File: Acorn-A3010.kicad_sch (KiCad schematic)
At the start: 0 parts

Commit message: progress schematic
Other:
- added sheet Audio (audio.kicad_sch)
- added sheet Keyboard (keyboard.kicad_sch)
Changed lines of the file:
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@@
+	)
+	(sheet
+		(at 109.22 82.55)
+		(size 21.59 17.78)
+		(fields_autoplaced yes)
+		(stroke
+			(width 0.1524)
+			(type solid)
+		)
+		(fill
+			(color 0 0 0 0.0000)
+		)
+		(property "Sheetname" "Audio"
+			(at 109.22 81.8384 0)
+			(effects
+				(font
+					(size 1.27 1.27)
+				)
+				(justify left bottom)
+			)
+		)
+		(property "Sheetfile" "audio.kicad_sch"
+			(at 109.22 100.9146 0)
+			(effects
+				(font
+					(size 1.27 1.27)
+				)
+				(justify left top)
+			)
+		)
+		(instances
+			(project "Acorn-A3010"
+				(path "/999882f3-94f8-4a89-9093-27a47d0cb289"
+					(page "13")
+				)
+			)
+		)
 	)
 	(sheet
@@
 	)
 	(sheet
+		(at 133.35 127)
+		(size 21.59 16.51)
+		(fields_autoplaced yes)
+		(stroke
+			(width 0.1524)
+			(type solid)
+		)
+		(fill
+			(color 0 0 0 0.0000)
+		)
+		(property "Sheetname" "Keyboard"
+			(at 133.35 126.2884 0)
+			(effects
+				(font
+					(size 1.27 1.27)
+				)
+				(justify left bottom)
+			)
+		)
+		(property "Sheetfile" "keyboard.kicad_sch"
+			(at 133.35 144.0946 0)
+			(effects
+				(font
+					(size 1.27 1.27)
+				)
+				(justify left top)
+			)
+		)
+		(instances
+			(project "Acorn-A3010"
+				(path "/999882f3-94f8-4a89-9093-27a47d0cb289"
+					(page "12")
+				)
+			)
+		)
+	)
+	(sheet
 		(at 186.69 95.25)
 		(size 22.225 20.32)
@@
 	)
 	(sheet
-		(at 109.22 82.55)
+		(at 85.09 82.55)
 		(size 21.59 17.78)
 		(fields_autoplaced yes)
@@
 		)
 		(property "Sheetname" "Reset"
-			(at 109.22 81.8384 0)
+			(at 85.09 81.8384 0)
 			(effects
 				(font
@@
 		)
 		(property "Sheetfile" "reset.kicad_sch"
-			(at 109.22 100.9146 0)
-			(effects
-				(font
+			(at 85.09 100.9146 0)
+			(effects
+				(font

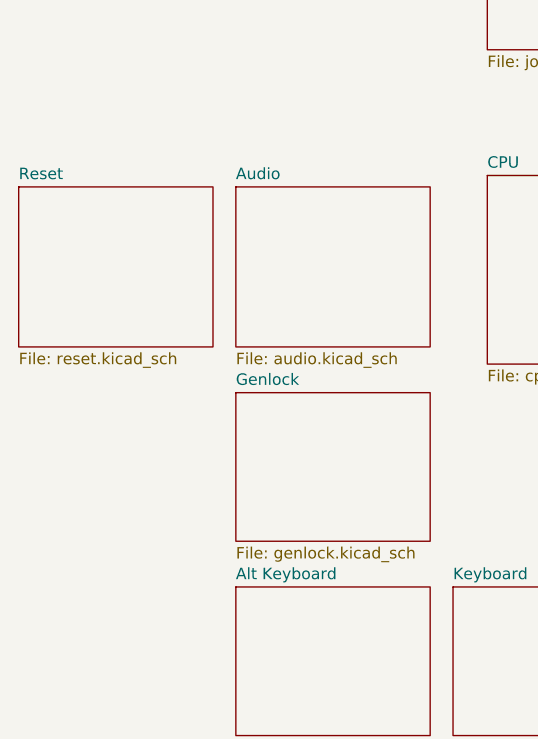
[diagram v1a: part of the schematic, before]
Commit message: add vcc clean filter
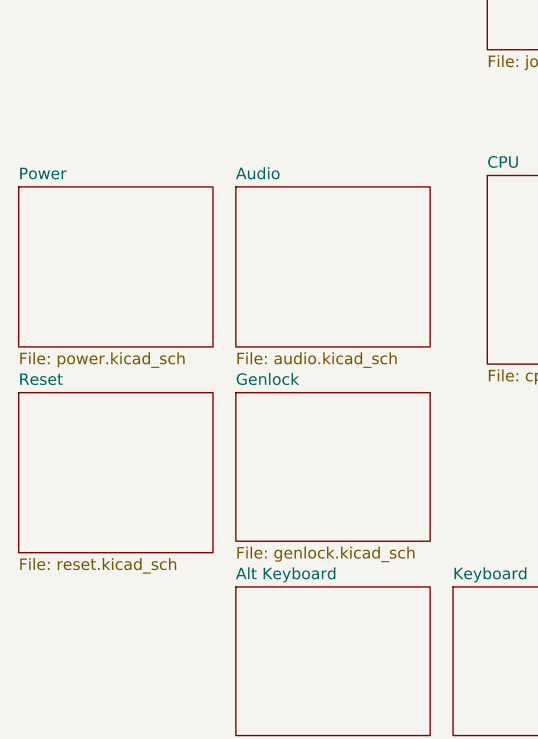
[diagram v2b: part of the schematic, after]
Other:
- added sheet Power (power.kicad_sch)
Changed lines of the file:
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@@
+	)
+	(sheet
+		(at 85.09 82.55)
+		(size 21.59 17.78)
+		(fields_autoplaced yes)
+		(stroke
+			(width 0.1524)
+			(type solid)
+		)
+		(fill
+			(color 0 0 0 0.0000)
+		)
+		(property "Sheetname" "Power"
+			(at 85.09 81.8384 0)
+			(effects
+				(font
+					(size 1.27 1.27)
+				)
+				(justify left bottom)
+			)
+		)
+		(property "Sheetfile" "power.kicad_sch"
+			(at 85.09 100.9146 0)
+			(effects
+				(font
+					(size 1.27 1.27)
+				)
+				(justify left top)
+			)
+		)
+		(instances
+			(project "Acorn-A3010"
+				(path "/999882f3-94f8-4a89-9093-27a47d0cb289"
+					(page "14")
+				)
+			)
+		)
 	)
 	(sheet
@@
 	)
 	(sheet
-		(at 85.09 82.55)
+		(at 85.09 105.41)
 		(size 21.59 17.78)
 		(fields_autoplaced yes)
@@
 		)
 		(property "Sheetname" "Reset"
-			(at 85.09 81.8384 0)
+			(at 85.09 104.6984 0)
 			(effects
 				(font
@@
 		)
 		(property "Sheetfile" "reset.kicad_sch"
-			(at 85.09 100.9146 0)
+			(at 85.09 123.7746 0)
 			(effects
 				(font

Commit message: fix perimter port positions
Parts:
- added H1, H2, H3, H4, H5, H6, H7, H8: MountingHole, MountingHole:MountingHole_3.2mm_M3, symbol Mechanical:MountingHole
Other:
- added sheet Video (video.kicad_sch)

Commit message: add rf video output
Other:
- added sheet Analog Video (tv.kicad_sch)
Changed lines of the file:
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@@
+	)
+	(sheet
+		(at 85.09 60.96)
+		(size 21.59 16.51)
+		(fields_autoplaced yes)
+		(stroke
+			(width 0.1524)
+			(type solid)
+		)
+		(fill
+			(color 0 0 0 0.0000)
+		)
+		(property "Sheetname" "Analog Video"
+			(at 85.09 60.2484 0)
+			(effects
+				(font
+					(size 1.27 1.27)
+				)
+				(justify left bottom)
+			)
+		)
+		(property "Sheetfile" "tv.kicad_sch"
+			(at 85.09 78.0546 0)
+			(effects
+				(font
+					(size 1.27 1.27)
+				)
+				(justify left top)
+			)
+		)
+		(instances
+			(project "Acorn-A3010"
+				(path "/999882f3-94f8-4a89-9093-27a47d0cb289"
+					(page "16")
+				)
+			)
+		)
 	)
 	(sheet

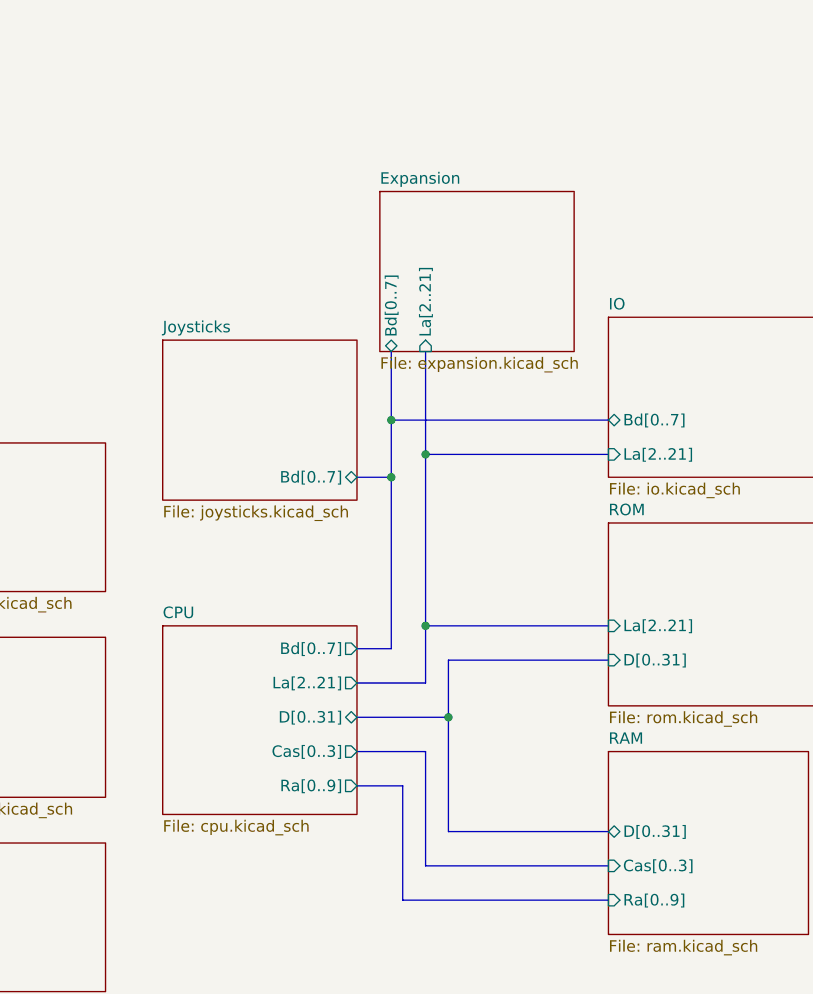
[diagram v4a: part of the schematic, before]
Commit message: add ide and rework onboard ram
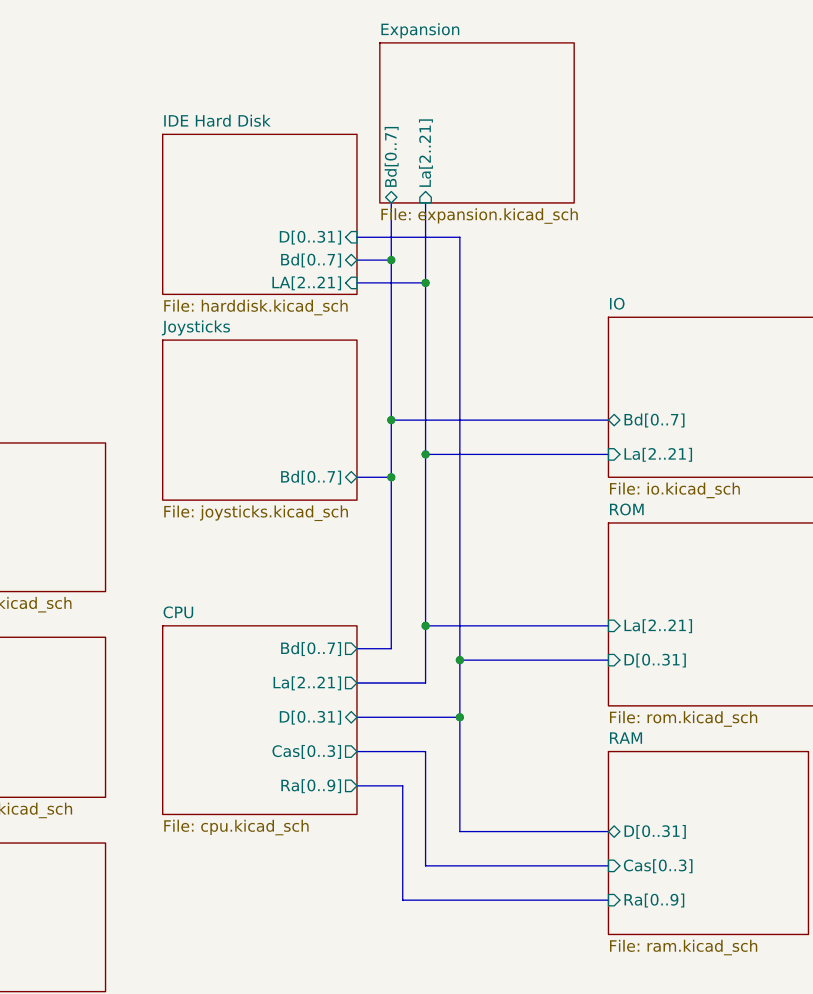
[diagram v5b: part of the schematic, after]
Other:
- added sheet IDE Hard Disk (harddisk.kicad_sch)
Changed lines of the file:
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@@
 (kicad_sch
-	(version 20231120)
+	(version 20250114)
 	(generator "eeschema")
-	(generator_version "8.0")
+	(generator_version "9.0")
 	(paper "A4")
 	(junction
@@
 	)
 	(junction
+		(at 170.18 91.44)
+		(diameter 0)
+		(color 0 0 0 0)
+	)
+	(junction
+		(at 170.18 85.09)
+		(diameter 0)
+		(color 0 0 0 0)
+	)
+	(junction
 		(at 162.56 58.42)
 		(diameter 0)
@@
 	)
 	(junction
-		(at 168.91 91.44)
+		(at 162.56 40.64)
+		(diameter 0)
+		(color 0 0 0 0)
+	)
+	(junction
+		(at 166.37 43.18)
 		(diameter 0)
 		(color 0 0 0 0)
@@
 	(bus
 		(pts
-			(xy 168.91 85.09) (xy 186.69 85.09)
-		)
-		(stroke
-			(width 0)
-			(type default)
-		)
-	)
-	(bus
-		(pts
 			(xy 158.75 99.06) (xy 163.83 99.06)
 		)
@@
 	(bus
 		(pts
+			(xy 162.56 40.64) (xy 162.56 58.42)
+		)
+		(stroke
+			(width 0)
+			(type default)
+		)
+	)
+	(bus
+		(pts
+			(xy 170.18 85.09) (xy 186.69 85.09)
+		)
+		(stroke
+			(width 0)
+			(type default)
+		)
+	)
+	(bus
+		(pts
 			(xy 166.37 107.95) (xy 186.69 107.95)
 		)
@@
 	(bus
 		(pts
-			(xy 166.37 50.8) (xy 166.37 62.23)
+			(xy 166.37 34.29) (xy 166.37 43.18)
 		)
 		(stroke
@@
 	(bus
 		(pts
-			(xy 158.75 91.44) (xy 168.91 91.44)
+			(xy 158.75 91.44) (xy 170.18 91.44)
+		)
+		(stroke
+			(width 0)
+			(type default)
+		)
+	)
+	(bus
+		(pts
+			(xy 158.75 40.64) (xy 162.56 40.64)
 		)
 		(stroke
@@
 	(bus
 		(pts
-			(xy 168.91 104.14) (xy 186.69 104.14)
-		)
-		(stroke
-			(width 0)
-			(type default)
-		)
-	)
-	(bus
-		(pts
-			(xy 168.91 85.09) (xy 168.91 91.44)
-		)
-		(stroke
-			(width 0)
-			(type default)
-		)
-	)
-	(bus
-		(pts
-			(xy 168.91 91.44) (xy 168.91 104.14)
-		)
-		(stroke
-			(width 0)
-			(type default)
-		)
-	)
-	(bus
-		(pts
-			(xy 162.56 50.8) (xy 162.56 58.42)
+			(xy 170.18 104.14) (xy 186.69 104.14)
+		)
+		(stroke
+			(width 0)
+			(type default)
+		)
+	)
+	(bus
+		(pts
+			(xy 170.18 38.1) (xy 170.18 85.09)
+		)
+		(stroke
+			(width 0)
+			(type default)
+		)
+	)
+	(bus
+		(pts
+			(xy 170.18 91.44) (xy 170.18 104.14)
+		)
+		(stroke
+			(width 0)
+			(type default)
+		)
+	)
+	(bus
+		(pts
+			(xy 162.56 34.29) (xy 162.56 40.64)
 		)
 		(stroke
@@
 	(bus
 		(pts
+			(xy 158.75 38.1) (xy 170.18 38.1)
+		)
+		(stroke
+			(width 0)
+			(type default)
+		)
+	)
+	(bus
+		(pts
+			(xy 166.37 43.18) (xy 166.37 62.23)
+		)
+		(stroke
+			(width 0)
+			(type default)
+		)
+	)
+	(bus
+		(pts
 			(xy 162.56 58.42) (xy 186.69 58.42)
+		)
+		(stroke
+			(width 0)
+			(type default)
+		)
+	)
+	(bus
+		(pts
+			(xy 158.75 43.18) (xy 166.37 43.18)
+		)
+		(stroke
+			(width 0)
+			(type default)
+		)
+	)
+	(bus
+		(pts
+			(xy 170.18 85.09) (xy 170.18 91.44)
 		)
 		(stroke
@@
 		)
 		(instances
-			(project ""
+			(project "Acorn-A3010"
 				(path "/999882f3-94f8-4a89-9093-27a47d0cb289"
 					(reference "H1")
@@
 		(at 109.22 82.55)
 		(size 21.59 17.78)
+		(exclude_from_sim no)
+		(in_bom yes)
+		(on_board yes)
+		(dnp no)
 		(fields_autoplaced yes)
 		(stroke
@@
 		(at 137.16 49.53)
 		(size 21.59 17.78)
+		(exclude_from_sim no)
+		(in_bom yes)
+		(on_board yes)
+		(dnp no)
 		(fields_autoplaced yes)
 		(stroke
@@
 		(at 133.35 127)
 		(size 21.59 16.51)
+		(exclude_from_sim no)
+		(in_bom yes)
+		(on_board yes)
+		(dnp no)
 		(fields_autoplaced yes)
 		(stroke
@@
 		(at 109.22 60.96)
 		(size 21.59 16.51)
+		(exclude_from_sim no)
+		(in_bom yes)
+		(on_board yes)
+		(dnp no)
 		(fields_autoplaced yes)
 		(stroke
@@
 		(at 85.09 60.96)
 		(size 21.59 16.51)
+		(exclude_from_sim no)
+		(in_bom yes)
+		(on_board yes)
+		(dnp no)
 		(fields_autoplaced yes)
 		(stroke
@@
 		(at 186.69 95.25)
 		(size 22.225 20.32)
+		(exclude_from_sim no)
+		(in_bom yes)
+		(on_board yes)
+		(dnp no)
 		(fields_autoplaced yes)
 		(stroke
@@
 				(path "/999882f3-94f8-4a89-9093-27a47d0cb289"
 					(page "4")
+				)
+			)
+		)
+	)
+	(sheet
+		(at 137.16 26.67)
+		(size 21.59 17.78)
+		(exclude_from_sim no)
+		(in_bom yes)
+		(on_board yes)
+		(dnp no)
+		(fields_autoplaced yes)
+		(stroke
+			(width 0.1524)
+			(type solid)
+		)
+		(fill
+			(color 0 0 0 0.0000)
+		)
+		(property "Sheetname" "IDE Hard Disk"
+			(at 137.16 25.9584 0)
+			(effects
+				(font
+					(size 1.27 1.27)
+				)
+				(justify left bottom)
+			)
+		)
+		(property "Sheetfile" "harddisk.kicad_sch"
+			(at 137.16 45.0346 0)
+			(effects
+				(font
+					(size 1.27 1.27)
+				)
+				(justify left top)
+			)
+		)
+		(pin "D[0..31]" input
+			(at 158.75 38.1 0)
+			(effects
+				(font
+					(size 1.27 1.27)
+				)
+				(justify right)
+			)
+		)
+		(pin "Bd[0..7]" bidirectional
+			(at 158.75 40.64 0)
+			(effects
+				(font
+					(size 1.27 1.27)
+				)
+				(justify right)
+			)
+		)
+		(pin "LA[2..21]" input
+			(at 158.75 43.18 0)
+			(effects
+				(font
+					(size 1.27 1.27)
+				)
+				(justify right)
+			)
+		)
+		(instances
+			(project "Acorn-A3010"
+				(path "/999882f3-94f8-4a89-9093-27a47d0cb289"
+					(page "17")
 				)
 			)
@@
 		(at 85.09 127)
 		(size 21.59 16.51)
+		(exclude_from_sim no)
+		(in_bom yes)
+		(on_board yes)
+		(dnp no)
 		(fields_autoplaced yes)
 		(stroke
@@
 		(at 109.22 105.41)
 		(size 21.59 16.51)
+		(exclude_from_sim no)
+		(in_bom yes)
+		(on_board yes)
+		(dnp no)
 		(fields_autoplaced yes)
 		(stroke
@@
 		(at 85.09 82.55)
 		(size 21.59 17.78)
+		(exclude_from_sim no)
+		(in_bom yes)
+		(on_board yes)
+		(dnp no)
 		(fields_autoplaced yes)
 		(stroke
@@
 		(at 137.16 81.28)
 		(size 21.59 20.955)
+		(exclude_from_sim no)
+		(in_bom yes)
+		(on_board yes)
+		(dnp no)
 		(fields_autoplaced yes)
 		(stroke
@@
 		(at 186.69 69.85)
 		(size 22.86 20.32)
+		(exclude_from_sim no)
+		(in_bom yes)
+		(on_board yes)
+		(dnp no)
 		(fields_autoplaced yes)
 		(stroke
@@
 		(at 85.09 105.41)
 		(size 21.59 16.51)
+		(exclude_from_sim no)
+		(in_bom yes)
+		(on_board yes)
+		(dnp no)
 		(fields_autoplaced yes)
 		(stroke
@@
 	)
 	(sheet
-		(at 161.29 33.02)
+		(at 161.29 16.51)
 		(size 21.59 17.78)
+		(exclude_from_sim no)
+		(in_bom yes)
+		(on_board yes)
+		(dnp no)
 		(fields_autoplaced yes)
 		(stroke
@@
 		)
 		(property "Sheetname" "Expansion"
-			(at 161.29 32.3084 0)
+			(at 161.29 15.7984 0)
 			(effects
 				(font
@@
 		)
 		(property "Sheetfile" "expansion.kicad_sch"
-			(at 161.29 51.3846 0)
+			(at 161.29 34.8746 0)
 			(effects
 				(font
@@
 		)
 		(pin "Bd[0..7]" bidirectional
-			(at 162.56 50.8 270)
+			(at 162.56 34.29 270)
 			(effects
 				(font
@@
 		)
 		(pin "La[2..21]" input
-			(at 166.37 50.8 270)
+			(at 166.37 34.29 270)
 			(effects
 				(font
@@
 		(at 186.69 46.99)
 		(size 22.86 17.78)
+		(exclude_from_sim no)
+		(in_bom yes)
+		(on_board yes)
+		(dnp no)
 		(fields_autoplaced yes)
 		(stroke
@@
 		(at 109.22 127)
 		(size 21.59 16.51)
+		(exclude_from_sim no)
+		(in_bom yes)
+		(on_board yes)
+		(dnp no)
 		(fields_autoplaced yes)
 		(stroke
@@
 		)
 	)
+	(embedded_fonts no)
 )
